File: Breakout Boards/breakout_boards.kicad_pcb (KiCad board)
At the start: 4 copper layers, 72.5 x 61.5 mm, 54 parts, among them J10 Conn_01x04_Pin, J11 Conn_01x04_Pin, J12 Conn_01x04_Pin, J13 Conn_01x04_Pin, J14 Conn_01x04_Pin, J15 Conn_01x04_Pin, J16 Conn_01x04_Pin, J17 Conn_01x04_Pin, J18 Conn_01x04_Pin, J19 Conn_01x04_Pin, J9 Conn_01x04_Pin, Q5 NPN BJT

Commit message: changed the board stackup for breakout boards
from 4 layer to 2 layer
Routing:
- added copper zone on B.Cu, net GND
- removed copper zone on In1.Cu, net GND
- removed copper zone on In2.Cu, net GND
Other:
- copper layers 4 -> 2

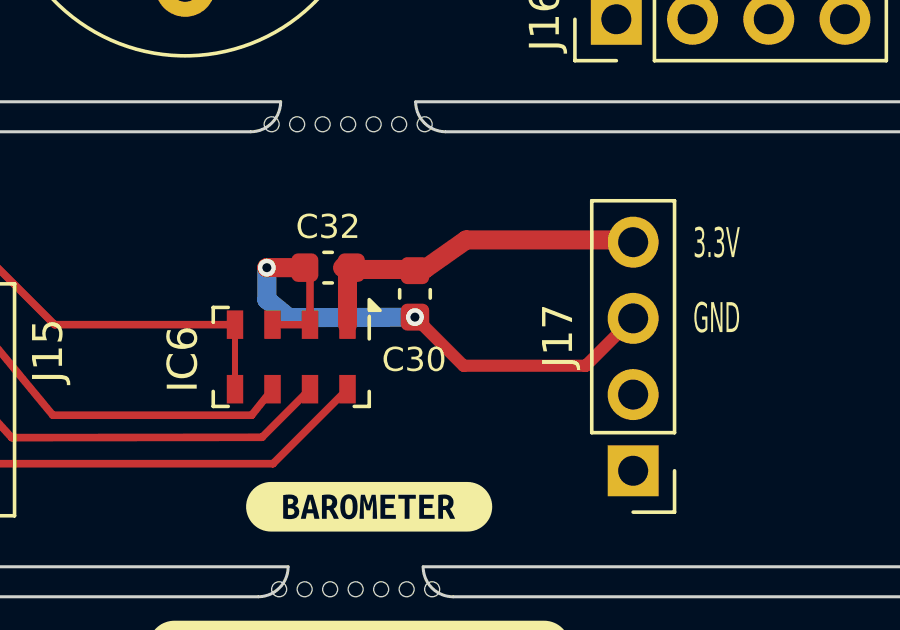
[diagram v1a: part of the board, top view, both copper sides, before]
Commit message: changed a via position for barometer
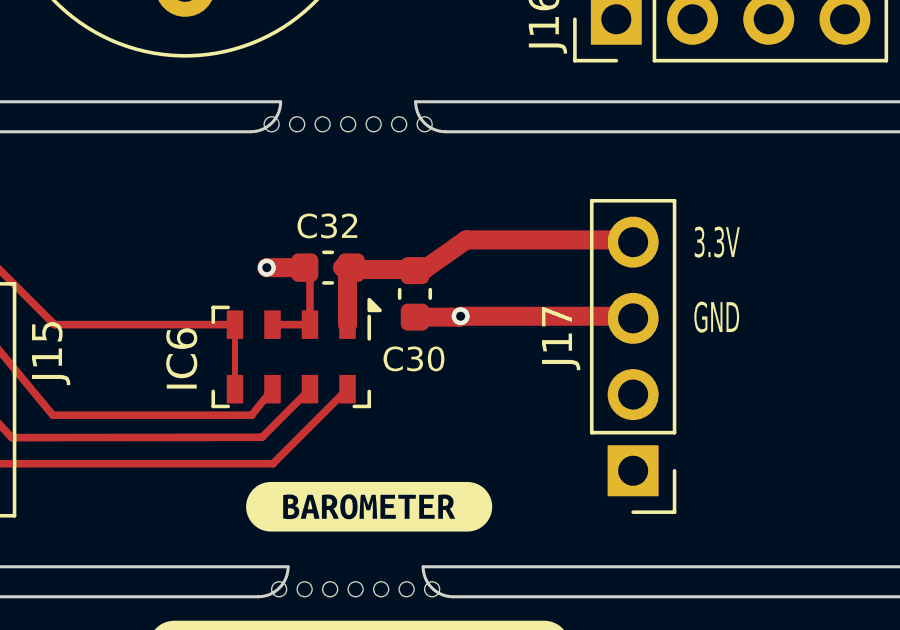
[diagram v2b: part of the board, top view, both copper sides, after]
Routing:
- net GND: track 85.7 -> 78.1 mm
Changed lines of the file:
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@@
 		(capping no)
 		(filling no)
-		(zone_defaults)
 		(pcbplotparams
 			(layerselection 0x00000000_00000000_5555555d_ff55ffff)
@@
 	)
 	(segment
-		(start 69.2272 83.379)
-		(end 70.8482 85)
-		(width 0.406)
-		(layer "F.Cu")
-		(net "GND")
-	)
-	(segment
 		(start 103.060103 83.722607)
 		(end 103.541102 83.722607)
@@
 	)
 	(segment
+		(start 76.43 83.35)
+		(end 76.5 83.42)
+		(width 0.635)
+		(layer "F.Cu")
+		(net "GND")
+	)
+	(segment
 		(start 64.290698 81.729302)
 		(end 64.29 81.73)
@@
 	)
 	(segment
-		(start 70.8482 85)
-		(end 74.92 85)
-		(width 0.406)
+		(start 69.2272 83.379)
+		(end 70.721 83.379)
+		(width 0.635)
 		(layer "F.Cu")
 		(net "GND")
@@
 	)
 	(segment
+		(start 70.721 83.379)
+		(end 70.75 83.35)
+		(width 0.635)
+		(layer "F.Cu")
+		(net "GND")
+	)
+	(segment
 		(start 76.1652 64.2536)
 		(end 76.2 64.2884)
@@
 	)
 	(segment
-		(start 74.92 85)
-		(end 76.5 83.42)
-		(width 0.406)
-		(layer "F.Cu")
-		(net "GND")
-	)
-	(segment
 		(start 71.279806 104.820803)
 		(end 73.278002 104.820803)
@@
 	)
 	(segment
+		(start 70.75 83.35)
+		(end 76.43 83.35)
+		(width 0.635)
+		(layer "F.Cu")
+		(net "GND")
+	)
+	(segment
 		(start 76.2 64.2884)
 		(end 77.6602 64.2884)
@@
 	)
 	(via
+		(at 70.75 83.35)
+		(size 0.6)
+		(drill 0.3)
+		(layers "F.Cu" "B.Cu")
+		(net "GND")
+	)
+	(via
 		(at 81.094 107.452403)
 		(size 0.6)
@@
 	)
 	(via
-		(at 69.2272 83.379)
-		(size 0.6)
-		(drill 0.3)
-		(layers "F.Cu" "B.Cu")
-		(net "GND")
-	)
-	(via
 		(at 84.756406 105.603203)
 		(size 0.6)
@@
 		(net "GND")
 	)
-	(segment
-		(start 65.03 83.4)
-		(end 69.2272 83.379)
-		(width 0.635)
-		(layer "B.Cu")
-		(net "GND")
-	)
-	(segment
-		(start 64.29 81.73)
-		(end 64.29 82.8)
-		(width 0.635)
-		(layer "B.Cu")
-		(net "GND")
-	)
-	(segment
-		(start 69.1672 83.439)
-		(end 69.2272 83.379)
-		(width 0.2)
-		(layer "B.Cu")
-		(net "GND")
-	)
-	(segment
-		(start 64.29 82.8)
-		(end 65.03 83.4)
-		(width 0.635)
-		(layer "B.Cu")
-		(net "GND")
-	)
